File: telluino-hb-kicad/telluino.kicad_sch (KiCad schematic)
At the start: 78 parts, among them J1 6P2C, J2 USB_A, Q1 MMBT3904, Q2 ZXTP2012Z, U1 LE9641PQC, U2 TISP61089BDR-S, U3 CH340C, U4 TXS0108EPWRG4

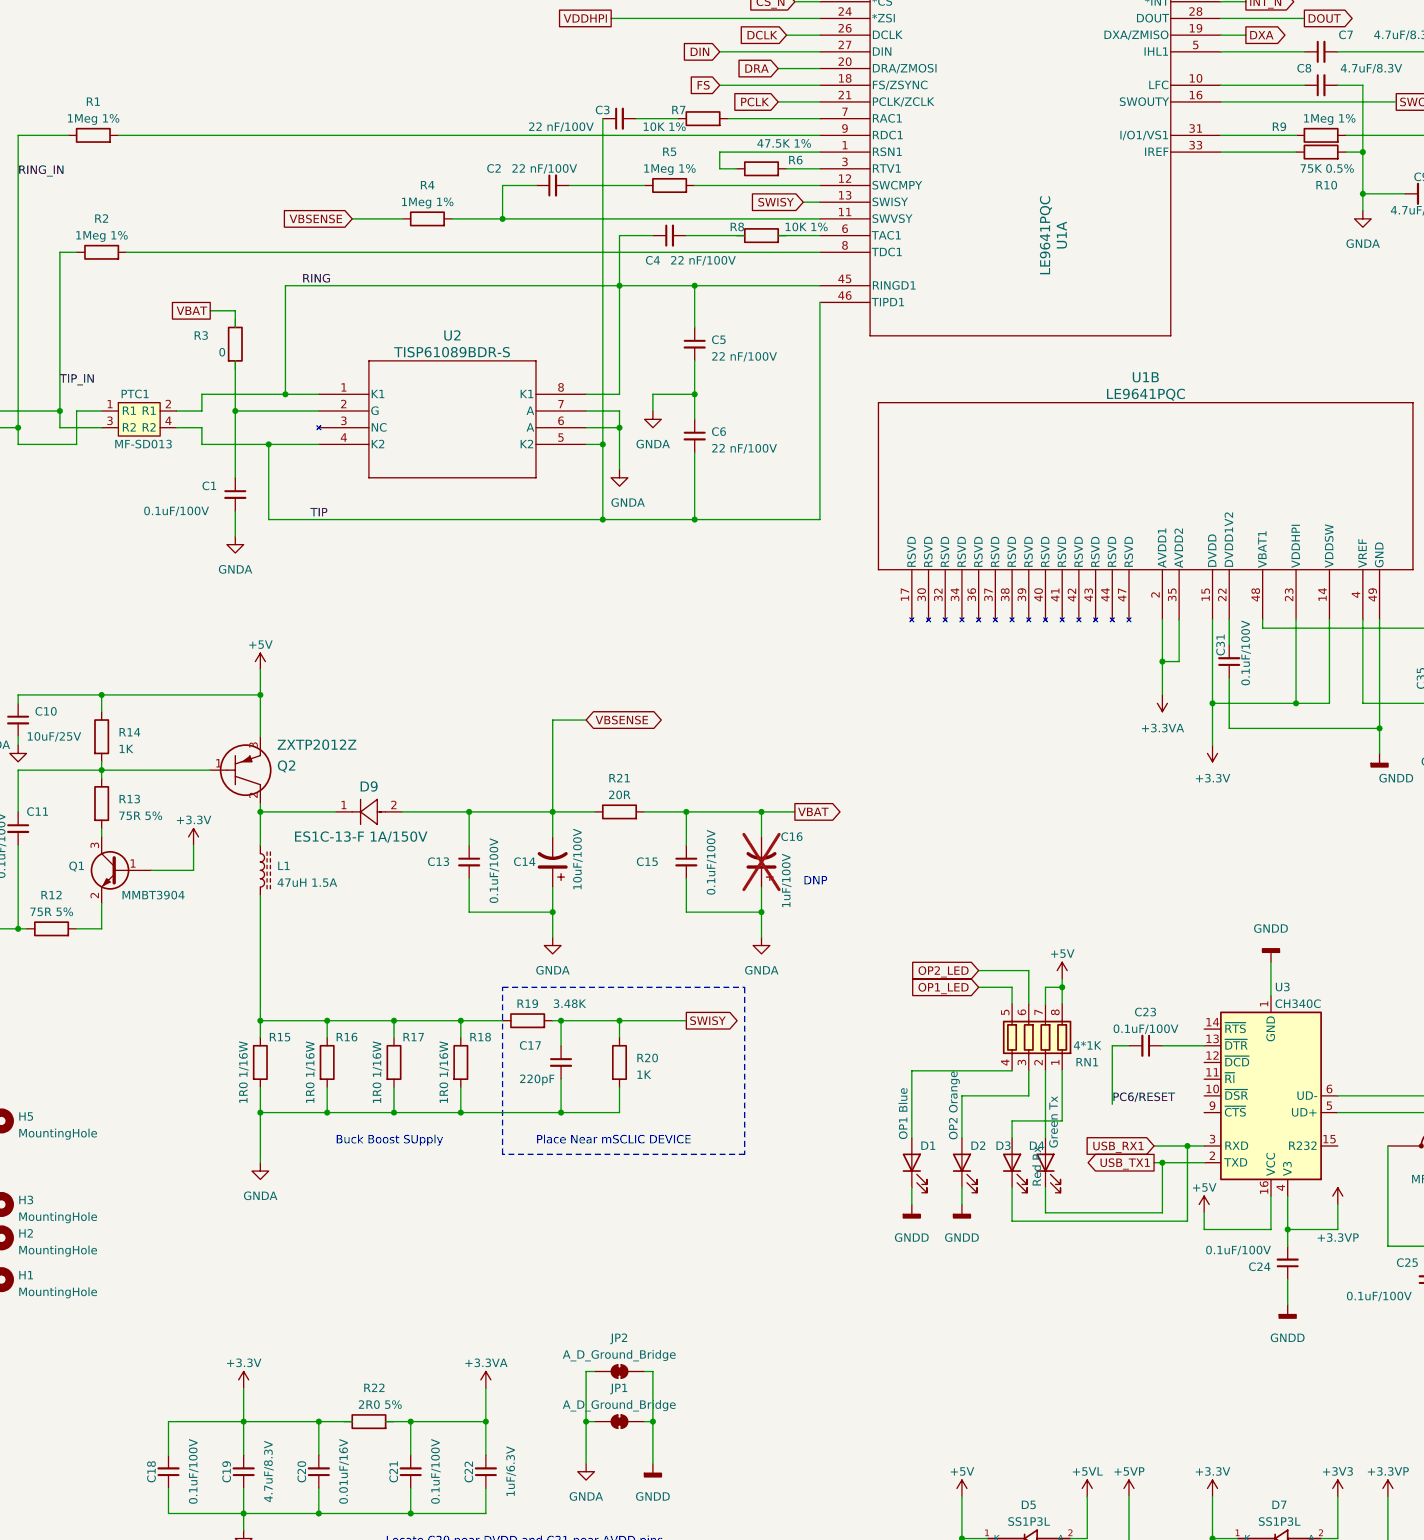
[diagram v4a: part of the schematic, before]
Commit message: revision after bom review and schematic review
U1 Pin 24 to connect to VCC
Review components to make is more affordable
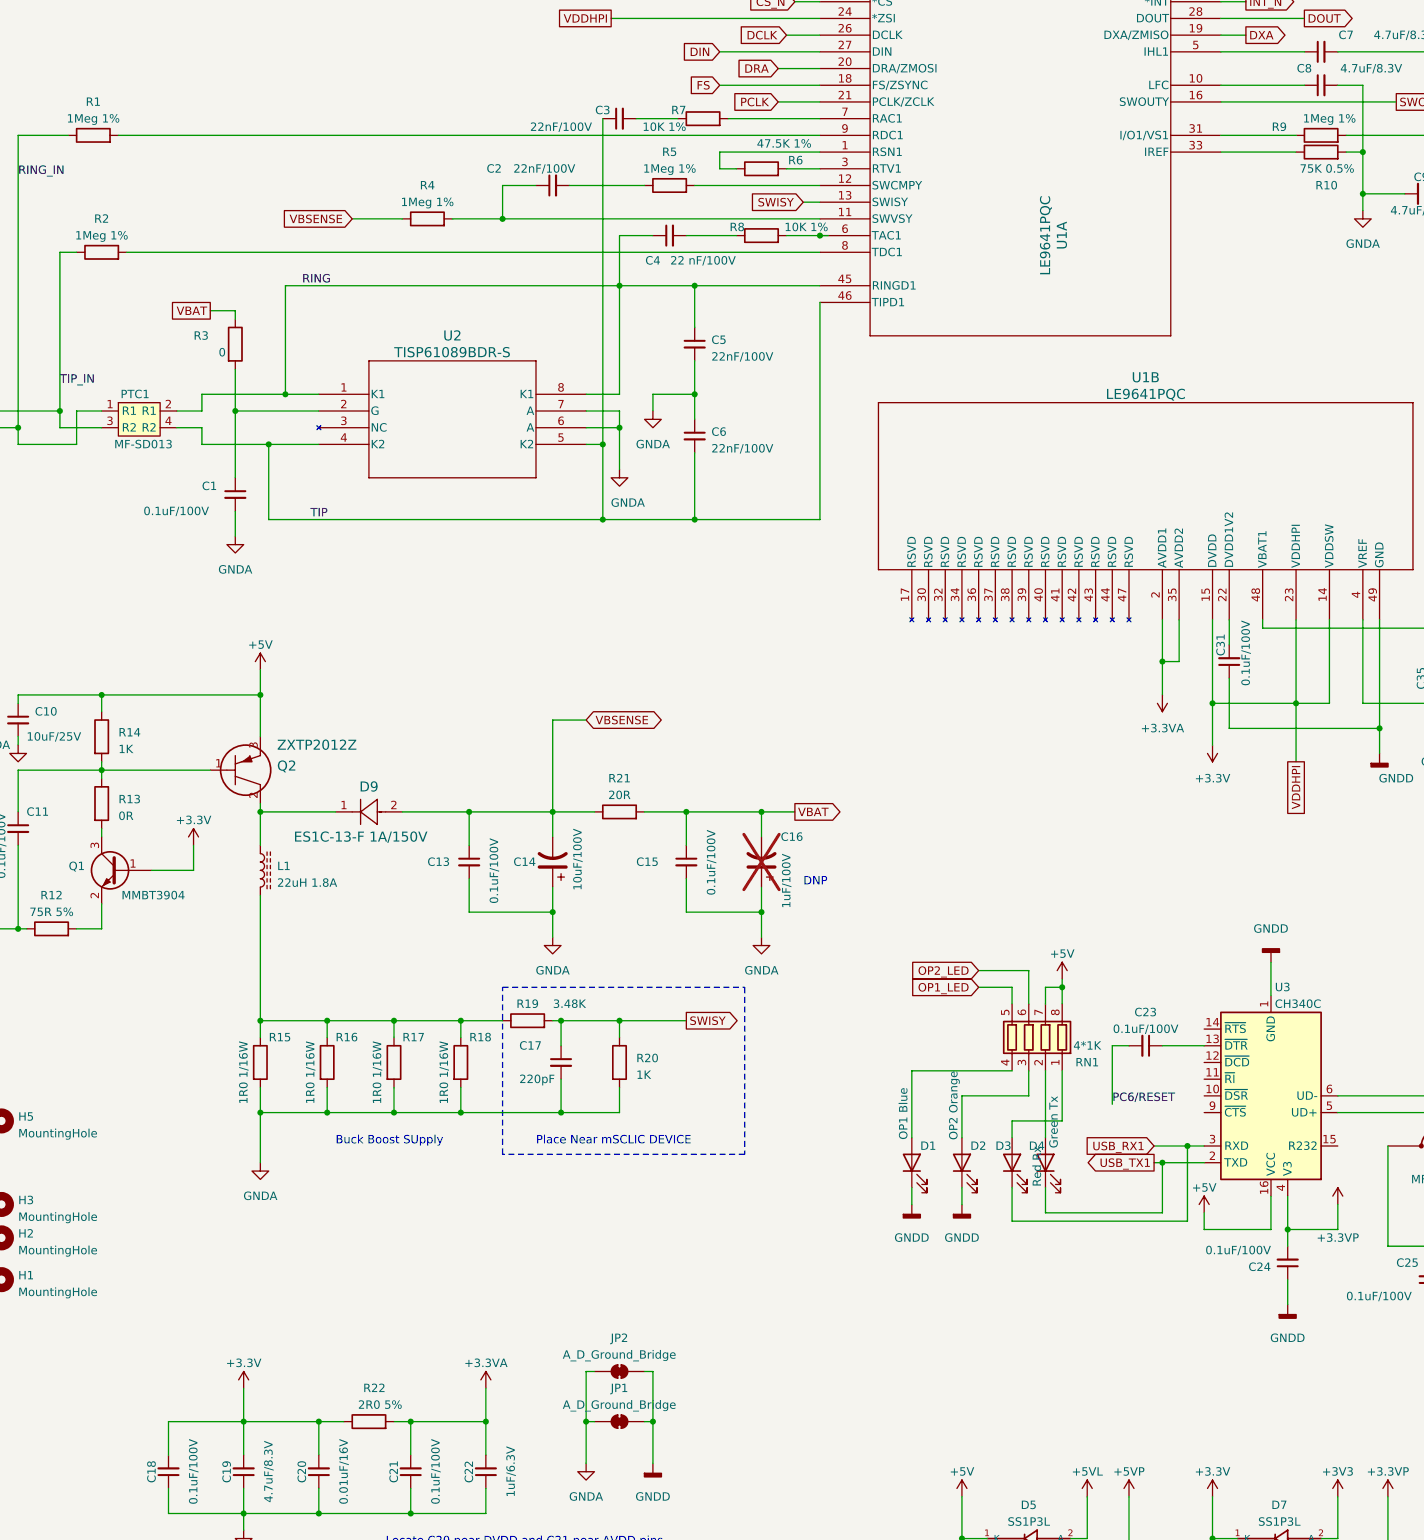
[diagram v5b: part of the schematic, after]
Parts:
- C2, C3, C5, C6: value 22 nF/100V -> 22nF/100V
- L1: value 47uH 1.5A -> 22uH 1.8A
- R13: value 75R 5% -> 0R
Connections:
- net VDDHPI is gone; now on net +3.3V: U1.24 (*ZSI)
- net +3.3V: now also R22.1
- net +3.3VA: now also R22.2
- net VBAT: now also R3.1
- net at C1.1, U2.2 (G): now also R3.2
- net at R8.1: now also C4.2
- net at R8.2: now also U1.6 (TAC1)
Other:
- title: Telluino Hardware-Bottom -> Telluino Uno Schield 
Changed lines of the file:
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@@
   (paper "A3")
   (title_block
-    (title "Telluino Hardware-Bottom")
-    (rev "1.0")
+    (title "Telluino Uno Schield ")
+    (rev "1.1")
     (company "Ksoft")
     (comment 1 "Hardware bottom to use with Arduino Uno and compatible boards")
@@
   (junction (at 99.06 184.15) (diameter 0) (color 0 0 0 0)
   )
+  (junction (at 163.83 64.77) (diameter 0) (color 0 0 0 0)
+  )
   (junction (at 76.2 259.08) (diameter 0) (color 0 0 0 0)
   )
@@
   (junction (at 88.9 198.12) (diameter 0) (color 0 0 0 0)
   )
+  (junction (at 87.63 245.11) (diameter 0) (color 0 0 0 0)
+  )
   (junction (at 144.78 88.9) (diameter 0) (color 0 0 0 0)
   )
@@
   (junction (at 264.16 218.44) (diameter 0) (color 0 0 0 0)
   )
-  (junction (at 87.63 245.11) (diameter 0) (color 0 0 0 0)
-  )
   (junction (at 248.92 139.7) (diameter 0) (color 0 0 0 0)
   )
@@
   (junction (at 109.22 198.12) (diameter 0) (color 0 0 0 0)
   )
-  (junction (at 41.91 170.18) (diameter 0) (color 0 0 0 0)
-  )
   (junction (at 101.6 245.11) (diameter 0) (color 0 0 0 0)
   )
+  (junction (at 41.91 170.18) (diameter 0) (color 0 0 0 0)
+  )
   (junction (at 87.63 259.08) (diameter 0) (color 0 0 0 0)
   )
@@
     (stroke (width 0) (type default))
   )
-  (wire (pts (xy 74.93 101.6) (xy 74.93 91.44))
-    (stroke (width 0) (type default))
-  )
   (wire (pts (xy 242.57 198.12) (xy 270.51 198.12))
     (stroke (width 0) (type default))
@@
     (stroke (width 0) (type default))
   )
-  (wire (pts (xy 74.93 83.82) (xy 74.93 91.44))
+  (wire (pts (xy 74.93 85.09) (xy 74.93 91.44))
     (stroke (width 0) (type default))
   )
@@
     (stroke (width 0) (type default))
   )
-  (wire (pts (xy 71.12 76.2) (xy 74.93 76.2))
-    (stroke (width 0) (type default))
-  )
   (wire (pts (xy 138.43 91.44) (xy 138.43 88.9))
     (stroke (width 0) (type default))
@@
     (stroke (width 0) (type default))
   )
+  (wire (pts (xy 74.93 76.2) (xy 74.93 77.47))
+    (stroke (width 0) (type default))
+  )
   (wire (pts (xy 48.26 67.31) (xy 48.26 91.44))
     (stroke (width 0) (type default))
@@
     (stroke (width 0) (type default))
   )
+  (wire (pts (xy 87.63 245.11) (xy 91.44 245.11))
+    (stroke (width 0) (type default))
+  )
   (wire (pts (xy 92.71 62.23) (xy 100.33 62.23))
     (stroke (width 0) (type default))
@@
     (stroke (width 0) (type default))
   )
+  (wire (pts (xy 236.22 135.89) (xy 236.22 144.78))
+    (stroke (width 0) (type default))
+  )
   (wire (pts (xy 355.6 64.77) (xy 377.19 64.77))
     (stroke (width 0) (type default))
@@
     (stroke (width 0) (type default))
   )
-  (wire (pts (xy 143.51 64.77) (xy 152.4 64.77))
-    (stroke (width 0) (type default))
-  )
   (wire (pts (xy 278.13 181.61) (xy 278.13 184.15))
     (stroke (width 0) (type default))
@@
     (stroke (width 0) (type default))
   )
-  (wire (pts (xy 97.79 245.11) (xy 101.6 245.11))
-    (stroke (width 0) (type default))
-  )
   (wire (pts (xy 69.85 88.9) (xy 82.55 88.9))
     (stroke (width 0) (type default))
@@
     (stroke (width 0) (type default))
   )
-  (wire (pts (xy 87.63 245.11) (xy 92.71 245.11))
-    (stroke (width 0) (type default))
-  )
   (wire (pts (xy 308.61 69.85) (xy 320.04 69.85))
     (stroke (width 0) (type default))
@@
     (stroke (width 0) (type default))
   )
+  (wire (pts (xy 74.93 91.44) (xy 74.93 101.6))
+    (stroke (width 0) (type default))
+  )
   (wire (pts (xy 74.93 106.68) (xy 74.93 110.49))
     (stroke (width 0) (type default))
@@
     (stroke (width 0) (type default))
   )
-  (wire (pts (xy 74.93 76.2) (xy 74.93 78.74))
-    (stroke (width 0) (type default))
-  )
   (wire (pts (xy 143.51 167.64) (xy 154.94 167.64))
     (stroke (width 0) (type default))
@@
     (stroke (width 0) (type default))
   )
+  (wire (pts (xy 165.1 64.77) (xy 163.83 64.77))
+    (stroke (width 0) (type default))
+  )
   (wire (pts (xy 309.88 52.07) (xy 320.04 52.07))
     (stroke (width 0) (type default))
@@
     (stroke (width 0) (type default))
   )
+  (wire (pts (xy 71.12 76.2) (xy 74.93 76.2))
+    (stroke (width 0) (type default))
+  )
+  (wire (pts (xy 158.75 64.77) (xy 163.83 64.77))
+    (stroke (width 0) (type default))
+  )
   (wire (pts (xy 64.77 255.27) (xy 64.77 259.08))
     (stroke (width 0) (type default))
@@
     (stroke (width 0) (type default))
   )
+  (wire (pts (xy 143.51 64.77) (xy 151.13 64.77))
+    (stroke (width 0) (type default))
+  )
   (wire (pts (xy 200.66 179.07) (xy 200.66 177.8))
     (stroke (width 0) (type default))
@@
     (stroke (width 0) (type default))
   )
+  (wire (pts (xy 99.06 245.11) (xy 101.6 245.11))
+    (stroke (width 0) (type default))
+  )
   (wire (pts (xy 133.35 186.69) (xy 133.35 184.15))
     (stroke (width 0) (type default))
@@
     (stroke (width 0) (type default))
   )
-  (wire (pts (xy 157.48 64.77) (xy 163.83 64.77))
-    (stroke (width 0) (type default))
-  )
   (wire (pts (xy 107.95 62.23) (xy 115.57 62.23))
     (stroke (width 0) (type default))
@@
     )
   )
+  (global_label "VDDHPI" (shape passive) (at 236.22 144.78 270) (fields_autoplaced)
+    (effects (font (size 1.27 1.27)) (justify right))
+    (property "Intersheetrefs" "${INTERSHEET_REFS}" (at 236.22 153.4084 90)
+      (effects (font (size 1.27 1.27)) (justify right) hide)
+    )
+  )
   (global_label "INT_N" (shape input) (at 335.28 196.85 180) (fields_autoplaced)
     (effects (font (size 1.27 1.27)) (justify right))
@@
       (effects (font (size 1.27 1.27)) (justify left))
     )
-    (property "Value" "47uH 1.5A" (at 81.28 163.195 0)
+    (property "Value" "22uH 1.8A" (at 81.28 163.195 0)
       (effects (font (size 1.27 1.27)) (justify left))
     )
@@
       (effects (font (size 1.27 1.27)) (justify left))
     )
-    (property "Value" "22 nF/100V" (at 147.32 83.1913 0)
+    (property "Value" "22nF/100V" (at 147.32 83.1913 0)
       (effects (font (size 1.27 1.27)) (justify left))
     )
@@
       (effects (font (size 1.27 1.27)))
     )
-    (property "Value" "22 nF/100V" (at 124.46 48.26 90)
+    (property "Value" "22nF/100V" (at 124.46 48.26 90)
       (effects (font (size 1.27 1.27)))
     )
@@
       (effects (font (size 1.27 1.27)) (justify left))
     )
-    (property "Value" "22 nF/100V" (at 147.32 97.1613 0)
+    (property "Value" "22nF/100V" (at 147.32 97.1613 0)
       (effects (font (size 1.27 1.27)) (justify left))
     )
@@
       (effects (font (size 1.27 1.27)) (justify left))
     )
-    (property "Value" "75R 5%" (at 57.15 153.035 0)
+    (property "Value" "0R" (at 57.15 153.035 0)
       (effects (font (size 1.27 1.27)) (justify left))
     )
@@
       (effects (font (size 1.27 1.27)))
     )
-    (property "Value" "22 nF/100V" (at 121.92 54.61 90)
+    (property "Value" "22nF/100V" (at 121.92 54.61 90)
       (effects (font (size 1.27 1.27)))
     )

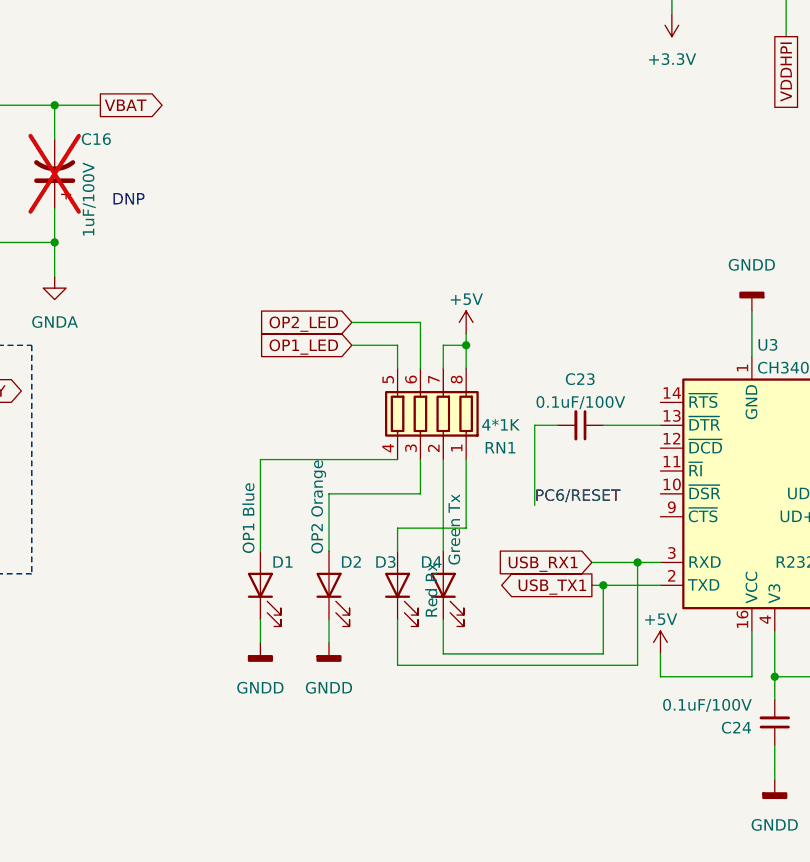
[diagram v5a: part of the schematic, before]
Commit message: reworn resistor array
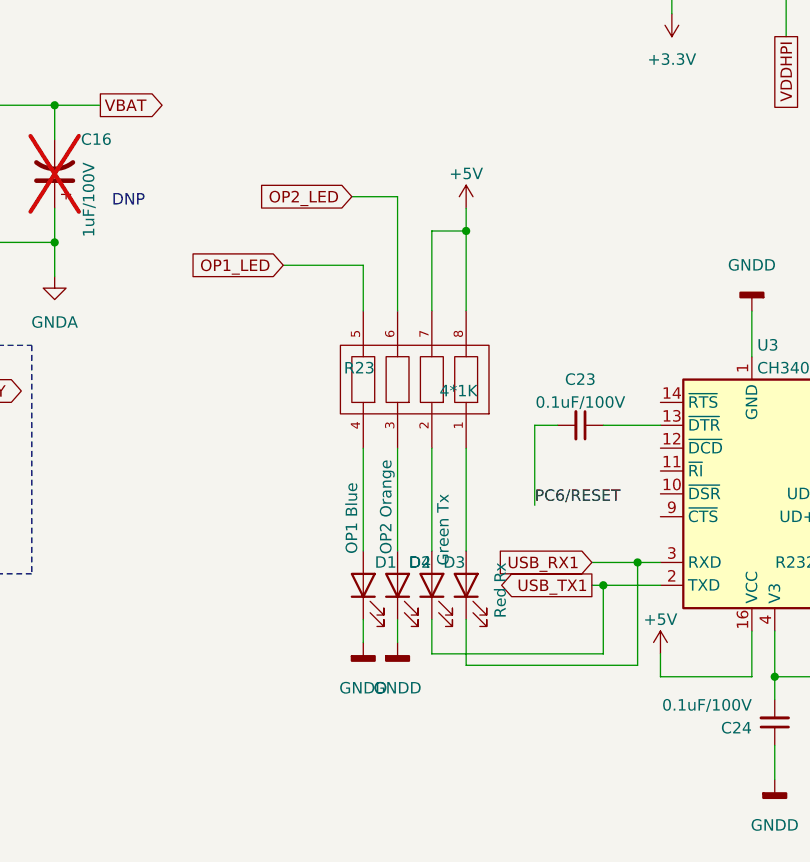
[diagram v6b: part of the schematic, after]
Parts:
- removed RN1: 4*1K, my_lib:SOIC127P780X210-8N, symbol Device:R_Pack04
- added R23: 4*1K, RESCAXE80P320X160X70-8N, symbol YC164:YC164-FR-071KL
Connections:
- net +5V: now also R23.7, R23.8
- net OP1_LED: now also R23.5
- net OP2_LED: now also R23.6
- net at D4.2 (A): now also R23.2
- net at D3.2 (A): now also R23.1
- net at D2.2 (A): now also R23.3
- net at D1.2 (A): now also R23.4
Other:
- moved on the sheet: D1, D2, D3, D4

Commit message: update after first review
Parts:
- C1, C11, C13, C15, C18, C21, C23, C24, C25, C31, C35: value 0.1uF/100V -> 100nF/100V
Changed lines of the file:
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@@
       (effects (font (size 1.27 1.27)))
     )
-    (property "Value" "0.1uF/100V" (at 260.35 130.81 90)
+    (property "Value" "100nF/100V" (at 260.35 130.81 90)
       (effects (font (size 1.27 1.27)))
     )
@@
       (effects (font (size 1.27 1.27)))
     )
-    (property "Value" "0.1uF/100V" (at 228.6 128.27 90)
+    (property "Value" "100nF/100V" (at 228.6 128.27 90)
       (effects (font (size 1.27 1.27)))
     )
@@
       (effects (font (size 1.27 1.27)) (justify right))
     )
-    (property "Value" "0.1uF/100V" (at 243.84 226.06 0)
+    (property "Value" "100nF/100V" (at 243.84 226.06 0)
       (effects (font (size 1.27 1.27)) (justify right))
     )
@@
       (effects (font (size 1.27 1.27)))
     )
-    (property "Value" "0.1uF/100V" (at 213.3536 185.42 90)
+    (property "Value" "100nF/100V" (at 213.3536 185.42 90)
       (effects (font (size 1.27 1.27)))
     )
@@
       (effects (font (size 1.27 1.27)) (justify left))
     )
-    (property "Value" "0.1uF/100V" (at 147.32 165.1 90)
+    (property "Value" "100nF/100V" (at 147.32 165.1 90)
       (effects (font (size 1.27 1.27)) (justify left))
     )
@@
       (effects (font (size 1.27 1.27)) (justify left))
     )
-    (property "Value" "0.1uF/100V" (at 232.41 219.0687 0)
+    (property "Value" "100nF/100V" (at 232.41 219.0687 0)
       (effects (font (size 1.27 1.27)) (justify left))
     )
@@
       (effects (font (size 1.27 1.27)) (justify left))
     )
-    (property "Value" "0.1uF/100V" (at 39.37 162.56 90)
+    (property "Value" "100nF/100V" (at 39.37 162.56 90)
       (effects (font (size 1.27 1.27)) (justify left))
     )
@@
       (effects (font (size 1.27 1.27)) (justify left))
     )
-    (property "Value" "0.1uF/100V" (at 60.96 106.68 0)
+    (property "Value" "100nF/100V" (at 60.96 106.68 0)
       (effects (font (size 1.27 1.27)) (justify left))
     )
@@
       (effects (font (size 1.27 1.27)) (justify left))
     )
-    (property "Value" "0.1uF/100V" (at 114.3 166.37 90)
+    (property "Value" "100nF/100V" (at 114.3 166.37 90)
       (effects (font (size 1.27 1.27)) (justify left))
     )
@@
       (effects (font (size 1.27 1.27)))
     )
-    (property "Value" "0.1uF/100V" (at 105.41 252.73 90)
+    (property "Value" "100nF/100V" (at 105.41 252.73 90)
       (effects (font (size 1.27 1.27)))
     )
@@
       (effects (font (size 1.27 1.27)))
     )
-    (property "Value" "0.1uF/100V" (at 68.58 252.73 90)
-      (effects (font (size 1.27 1.27)))
-    )
+    (property "Value" "100nF/100V" (at 68.58 252.73 90)
+      (effects (font (size 1.27 1.27)))
+    )
